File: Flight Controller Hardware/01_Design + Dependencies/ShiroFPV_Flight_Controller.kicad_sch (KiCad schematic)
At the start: 112 parts, among them J1 GND, J10 TLM, J11 Video_Out, J12 Video_IN, J13 5V3, J14 RX3, J15 TX3, J16 GND3, J17 5V4, J18 RX4, J19 TX4, J2 GND, J20 GND4, J24 +5V, J25 RSSI, J26 GND5, J29 SBUS, J3 VBAT, J30 5V5, J31 RX5, J32 TX5, J33 RX6, J34 5V6, J35 GND6, J36 TX6, J37 10V, J38 RX1, J39 TX1, J4 VBAT, J40 GND1, J42 B-, J46 GND, J5 M1, J6 M2, J7 M3, J8 M4, J9 CUR, P1 USB_C_Plug_USB2.0, Q1 AO3401A, Q2 AO3400A, Q3 BC817W, U1 AT32F435RGT7, U10 AT7456, U3 ICM-20602, U4 BME280, U5 TPS54302, U6 TPS54302DDCR, U7 RT9013-33GB, U8 W25Q128JVS, Y2 27MHz

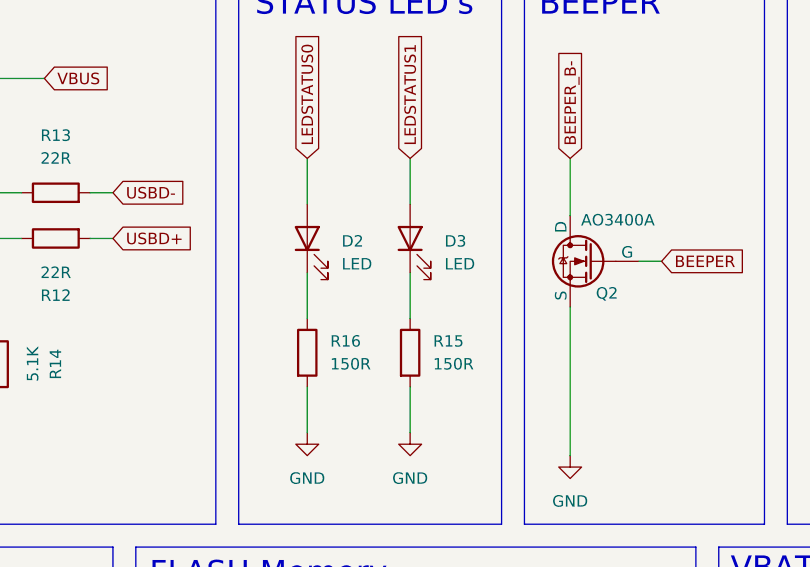
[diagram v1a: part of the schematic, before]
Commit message: Add backups; update KiCad project files
Add three timestamped project backup ZIPs for ShiroFPV_Flight_Controller. Update .kicad_prl to set active_layer from 0 to 2. Update .kicad_sch to remove fields_autoplaced for D2 and D3 and replace their Value fields from generic "LED" to specific component identifiers (C2986058 and C72038) with adjusted positions, keeping other properties intact. These changes keep project metadata in sync with schematic component naming and preserve recent backups.
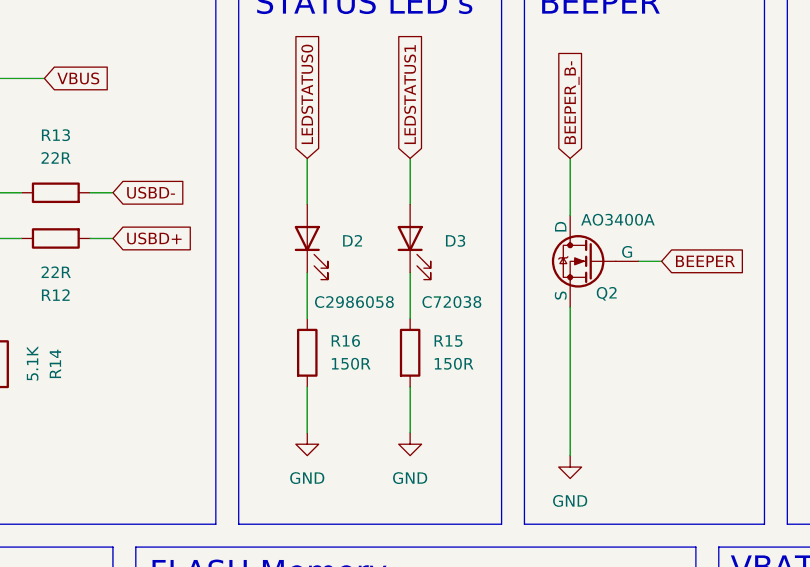
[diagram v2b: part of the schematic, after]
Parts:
- D2: value LED -> C2986058
- D3: value LED -> C72038
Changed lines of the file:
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@@
 		(on_board yes)
 		(dnp no)
-		(fields_autoplaced yes)
 		(property "Reference" "D2"
 			(at 265.43 119.6974 90)
@@
 			)
 		)
-		(property "Value" "LED"
-			(at 265.43 122.2374 90)
+		(property "Value" "C2986058"
+			(at 262.382 126.492 90)
 			(effects
 				(font
@@
 		(on_board yes)
 		(dnp no)
-		(fields_autoplaced yes)
 		(property "Reference" "D3"
 			(at 276.86 119.6974 90)
@@
 			)
 		)
-		(property "Value" "LED"
-			(at 276.86 122.2374 90)
+		(property "Value" "C72038"
+			(at 274.32 126.492 90)
 			(effects
 				(font
